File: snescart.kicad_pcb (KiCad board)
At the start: 2 copper layers, 101.6 x 37.3 mm, 7 parts, among them P1 CASSETTE, U1 27C080

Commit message: imperial mil cart edge
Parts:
- P1: footprint Library:CartEdge -> Library:ImperialCart
- moved P1 1.51 mm to (146.3, 144.0)

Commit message: footprint again
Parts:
- moved C2 0.64 mm to (176.5, 116.1)
- moved P1 0.25 mm to (146.6, 144.0)
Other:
- outline, holes or cut-outs redrawn

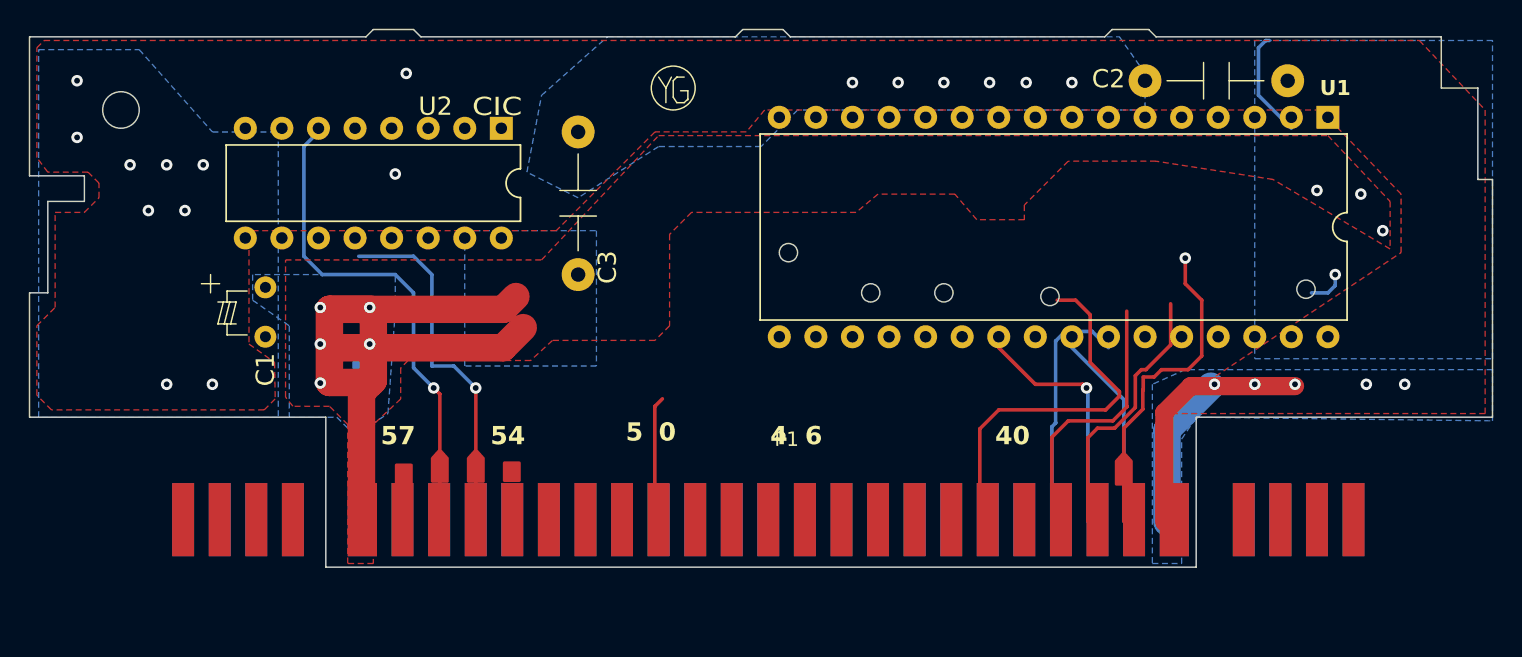
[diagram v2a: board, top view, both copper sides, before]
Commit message: move edge
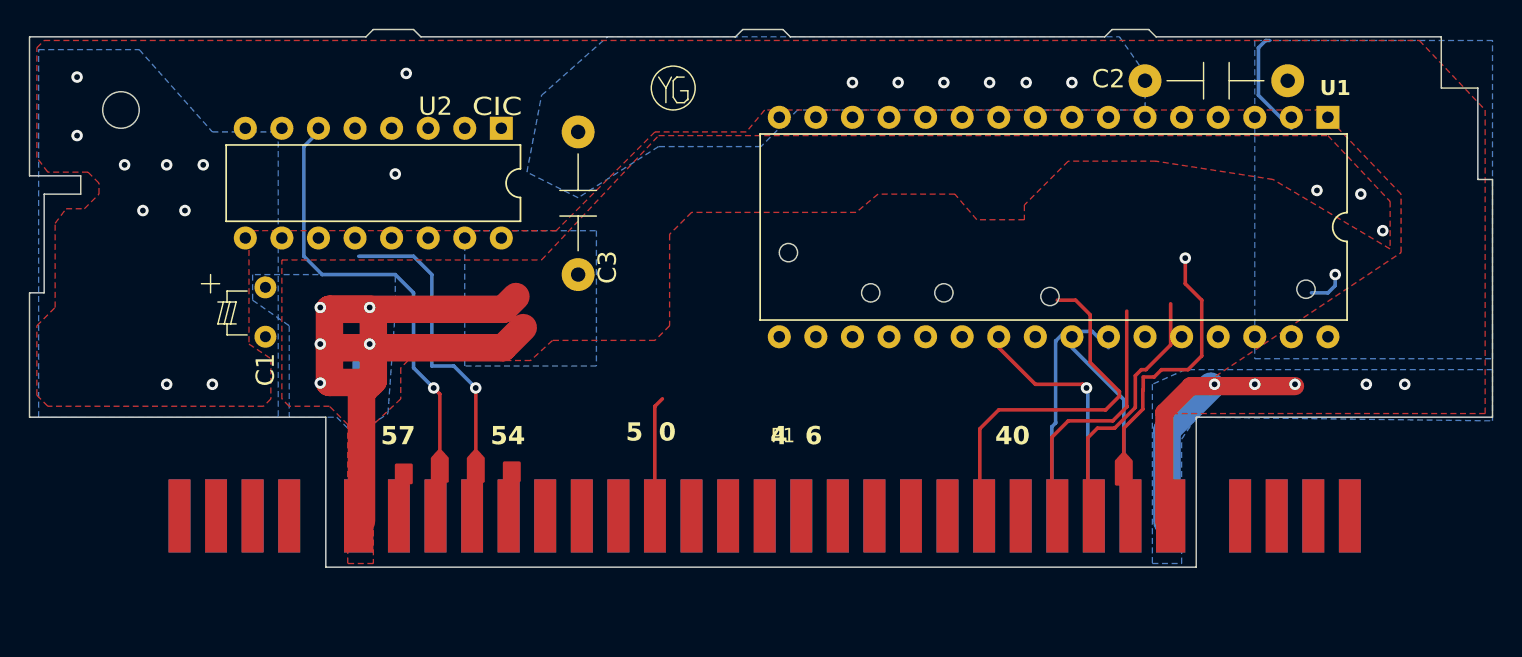
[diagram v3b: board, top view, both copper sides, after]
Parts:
- moved P1 0.36 mm to (146.3, 143.8)
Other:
- outline, holes or cut-outs redrawn
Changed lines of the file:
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@@
   )
   (footprint "Library:ImperialCart" (layer "F.Cu")
-    (at 146.558 144.018)
+    (at 146.304 143.764)
     (property "Sheetfile" "snescart.kicad_sch")
     (property "Sheetname" "")
@@
     )
     (dimension (type aligned) (layer "F.SilkS")
-      (pts (xy 116.713 149.098) (xy 173.863 149.098))
+      (pts (xy 116.459 148.844) (xy 173.609 148.844))
       (height 5.08)
-      (gr_text "2.2500 in" (at 145.288 153.078) (layer "F.SilkS")
+      (gr_text "57.1500 mm" (at 145.034 152.824) (layer "F.SilkS")
         (effects (font (size 1 1) (thickness 0.1)))
       )
@@
   (gr_rect (start 114 143.384) (end 175.5 150.114)
     (stroke (width 0.15) (type solid)) (fill solid) (layer "F.Mask"))
+  (gr_poly
+    (pts
+      (xy 104.14 117.348)
+      (xy 104.14 118.872)
+      (xy 102.616 118.11)
+    )
+    (stroke (width 0.2) (type solid)) (fill solid) (layer "F.Mask"))
   (gr_line (start 93.98 139.446) (end 114.554 139.446)
     (stroke (width 0.1) (type default)) (layer "Edge.Cuts"))
-  (gr_line (start 95.25 130.81) (end 95.25 124.46)
+  (gr_line (start 94.996 130.81) (end 94.996 123.952)
     (stroke (width 0.1) (type default)) (layer "Edge.Cuts"))
   (gr_line (start 146.304 112.522) (end 143.51 112.522)
@@
   (gr_line (start 175.006 139.446) (end 175.006 149.86)
     (stroke (width 0.1) (type default)) (layer "Edge.Cuts"))
-  (gr_line (start 97.79 124.46) (end 97.79 122.682)
+  (gr_line (start 97.536 123.952) (end 97.536 122.682)
     (stroke (width 0.1) (type default)) (layer "Edge.Cuts"))
   (gr_circle (center 164.846 131.064) (end 165.481 131.064)
@@
   (gr_line (start 175.26 149.86) (end 175.26 149.86)
     (stroke (width 0.1) (type default)) (layer "Edge.Cuts"))
-  (gr_line (start 95.25 124.46) (end 97.79 124.46)
+  (gr_line (start 94.996 123.952) (end 97.536 123.952)
     (stroke (width 0.1) (type default)) (layer "Edge.Cuts"))
   (gr_circle (center 152.4 130.81) (end 152.4 130.175)
@@
   (gr_line (start 114.554 139.446) (end 114.554 149.86)
     (stroke (width 0.1) (type default)) (layer "Edge.Cuts"))
-  (gr_line (start 93.98 130.81) (end 95.25 130.81)
+  (gr_line (start 93.98 130.81) (end 94.996 130.81)
     (stroke (width 0.1) (type default)) (layer "Edge.Cuts"))
   (gr_line (start 93.98 113.03) (end 93.98 122.682)
@@
   (gr_line (start 143.51 112.522) (end 143.002 113.03)
     (stroke (width 0.1) (type default)) (layer "Edge.Cuts"))
-  (gr_line (start 97.79 122.682) (end 93.98 122.682)
+  (gr_line (start 97.536 122.682) (end 93.98 122.682)
     (stroke (width 0.1) (type default)) (layer "Edge.Cuts"))
   (gr_circle (center 100.33 118.11) (end 100.33 119.38)
@@
   (segment (start 172.788 139.124) (end 174.625 137.287) (width 1.27) (layer "F.Cu") (net 1))
   (segment (start 176.022 137.287) (end 181.864 137.287) (width 1.27) (layer "F.Cu") (net 1))
-  (via (at 97.282 116.078) (size 0.8) (drill 0.4) (layers "F.Cu" "B.Cu") (free) (net 1))
+  (via (at 97.282 115.824) (size 0.8) (drill 0.4) (layers "F.Cu" "B.Cu") (free) (net 1))
   (via (at 160.655 116.205) (size 0.8) (drill 0.4) (layers "F.Cu" "B.Cu") (free) (net 1))
   (via (at 189.484 137.16) (size 0.8) (drill 0.4) (layers "F.Cu" "B.Cu") (net 1))
   (via (at 120.142 115.57) (size 0.8) (drill 0.4) (layers "F.Cu" "B.Cu") (free) (net 1))
   (via (at 106.68 137.16) (size 0.8) (drill 0.4) (layers "F.Cu" "B.Cu") (free) (net 1))
-  (via (at 102.235 125.095) (size 0.8) (drill 0.4) (layers "F.Cu" "B.Cu") (free) (net 1))
+  (via (at 101.854 125.095) (size 0.8) (drill 0.4) (layers "F.Cu" "B.Cu") (free) (net 1))
   (via (at 181.864 137.16) (size 0.8) (drill 0.4) (layers "F.Cu" "B.Cu") (net 1))
   (via (at 151.13 116.205) (size 0.8) (drill 0.4) (layers "F.Cu" "B.Cu") (free) (net 1))
   (via (at 104.775 125.095) (size 0.8) (drill 0.4) (layers "F.Cu" "B.Cu") (free) (net 1))
   (via (at 176.276 137.16) (size 0.8) (drill 0.4) (layers "F.Cu" "B.Cu") (net 1))
-  (via (at 97.282 120.015) (size 0.8) (drill 0.4) (layers "F.Cu" "B.Cu") (free) (net 1))
+  (via (at 97.282 119.888) (size 0.8) (drill 0.4) (layers "F.Cu" "B.Cu") (free) (net 1))
   (via (at 179.07 137.16) (size 0.8) (drill 0.4) (layers "F.Cu" "B.Cu") (net 1))
   (via (at 154.305 116.205) (size 0.8) (drill 0.4) (layers "F.Cu" "B.Cu") (free) (net 1))
@@
   (via (at 157.48 116.205) (size 0.8) (drill 0.4) (layers "F.Cu" "B.Cu") (free) (net 1))
   (via (at 163.195 116.205) (size 0.8) (drill 0.4) (layers "F.Cu" "B.Cu") (free) (net 1))
-  (via (at 100.965 121.92) (size 0.8) (drill 0.4) (layers "F.Cu" "B.Cu") (free) (net 1))
+  (via (at 100.584 121.92) (size 0.8) (drill 0.4) (layers "F.Cu" "B.Cu") (free) (net 1))
   (segment (start 172.975 146.733) (end 172.975 140.334) (width 1.905) (layer "B.Cu") (net 1))
   (segment (start 172.975 140.334) (end 176.022 137.287) (width 1.905) (layer "B.Cu") (net 1))
@@
         (xy 116.078 139.954)
         (xy 114.808 138.684)
-        (xy 112.268 138.684)
-        (xy 111.76 138.049)
-        (xy 111.76 128.524)
+        (xy 112.014 138.684)
+        (xy 111.506 138.176)
+        (xy 111.506 128.524)
         (xy 129.54 128.524)
         (xy 137.668 119.888)
@@
         (xy 94.488 133.096)
         (xy 95.758 131.826)
-        (xy 95.758 125.222)
-        (xy 97.79 125.222)
-        (xy 98.806 124.206)
+        (xy 95.758 125.984)
+        (xy 96.52 124.968)
+        (xy 97.79 124.968)
+        (xy 98.806 123.952)
         (xy 98.806 123.19)
         (xy 98.044 122.428)
@@
         (xy 109.22 126.492)
         (xy 109.22 134.366)
-        (xy 110.998 135.636)
-        (xy 111.041818 138.176)
-        (xy 110.272515 138.938)
-        (xy 95.504 138.938)
+        (xy 110.744 135.382)
+        (xy 110.744 138.176)
+        (xy 110.236 138.684)
+        (xy 95.25 138.684)
       )
     )

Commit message: 38mil spacing smh
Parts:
- moved P1 2.82 mm to (143.5, 143.8)

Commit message: aaaaaaa
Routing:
- net VCC: track 65.6 -> 0.13 mm
- net Net-(P1-CIC3): track 34.7 -> 9.45 mm
- net GND: track 28.2 -> 5.84 mm
- net Net-(P1-CIC1): track 24.9 -> 9.27 mm
- net Net-(P1-A11): track 13.6 -> 0.00 mm
- net Net-(P1-A9): track 17.1 -> 6.57 mm
- net Net-(P1-A12): track 22.5 -> 16.1 mm
- net Net-(P1-A19): track 2.62 -> 0.00 mm
- net Net-(P1-D4): track 9.90 -> 8.29 mm
- net Net-(P1-A16): track 33.8 -> 32.5 mm
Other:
- outline, holes or cut-outs redrawn

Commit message: expand
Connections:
- P1 pad 1: (no net) -> unconnected-(P1-MCK_21M-Pad1)
- P1 pad 2: (no net) -> unconnected-(P1-EXPAND-Pad2)
- P1 pad 28: (no net) -> unconnected-(P1-PA0-Pad28)
- P1 pad 29: (no net) -> unconnected-(P1-PA2-Pad29)
- P1 pad 3: (no net) -> unconnected-(P1-PA6-Pad3)
- P1 pad 30: (no net) -> unconnected-(P1-PA4-Pad30)
- P1 pad 31: (no net) -> unconnected-(P1-SOUND-L-Pad31)
- P1 pad 32: (no net) -> unconnected-(P1-WRAMSEL-Pad32)
- P1 pad 33: (no net) -> unconnected-(P1-REFRESH-Pad33)
- P1 pad 34: (no net) -> unconnected-(P1-PA7-Pad34)
- P1 pad 35: (no net) -> unconnected-(P1-PAWR-Pad35)
- P1 pad 4: (no net) -> unconnected-(P1-PARD-Pad4)
- P1 pad 59: (no net) -> unconnected-(P1-PA1-Pad59)
- P1 pad 60: (no net) -> unconnected-(P1-PA3-Pad60)
- P1 pad 61: (no net) -> unconnected-(P1-PA5-Pad61)
- P1 pad 62: (no net) -> unconnected-(P1-SOUND-R-Pad62)
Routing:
- net VCC: track 0.13 -> 9.34 mm, vias 8 -> 11

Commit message: cap
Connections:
- C3 pad 1: unconnected-(C3-Pad1) -> GND
- C3 pad 2: unconnected-(C3-Pad2) -> VCC
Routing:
- net Net-(P1-D4): track 8.29 -> 28.2 mm, vias 0 -> 1
- net Net-(P1-A11): track 0.00 -> 13.8 mm
- net Net-(P1-D7): track 0.00 -> 10.4 mm
- net Net-(P1-D6): track 0.00 -> 9.72 mm
- net VCC: track 9.34 -> 18.7 mm
- net Net-(P1-D5): track 0.00 -> 8.86 mm
- net GND: track 5.84 -> 13.4 mm
- net Net-(P1-A10): track 16.6 -> 9.67 mm
- net Net-(P1-A9): track 6.57 -> 11.1 mm
- net unconnected-(P1-WR-Pad54): track 0.00 -> 3.38 mm
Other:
- outline, holes or cut-outs redrawn
